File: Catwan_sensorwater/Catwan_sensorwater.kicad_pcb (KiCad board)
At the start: 2 copper layers, 40 parts, among them J1 SENSOR 1, J10 VSP, J2 SENSOR 2, J3 SENSOR 3, J4 BATT, J5 USB_B, J6 Conn_01x04, J7 Serial, J8 Conn_01x03_Female, J9 SENSOR 4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

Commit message: Inicio PCB
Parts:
- added U5: 74HC4052, Package_SO:SOIC-16_3.9x9.9mm_P1.27mm, F.Cu at (495.9, -68.6)
- J7: value Serial -> Conn_01x03; footprint TerminalBlock_Phoenix:TerminalBlock_Phoenix_PT-1,5-2-3.5-H_1x02_P3.50mm_Horizontal -> Connector_PinHeader_2.54mm:PinHeader_1x03_P2.54mm_Vertical
- U4: footprint Package_TO_SOT_SMD:SOT-223 -> Package_TO_SOT_SMD:SOT-23-5
- moved Q2 113.8 mm to (529.6, -58.4)
- moved Q4 98.4 mm to (518.2, -40.0)
- moved D10 86.8 mm to (495.9, -92.7)
- moved J3 81.3 mm to (511.2, -113.0)
- moved J8 80.7 mm to (520.7, -101.0)
- moved J1 79.4 mm to (505.5, -27.9)
- moved Q3 76.5 mm to (502.9, -65.4)
- moved R2 71.1 mm to (387.6, -97.2)
- moved J9 67.8 mm to (516.6, -75.6)
- moved D8 66.1 mm to (461.3, -101.0)
- moved J2 63.2 mm to (513.1, -61.0)
- moved C1 60.7 mm to (398.4, -55.9)
- moved C7 57.6 mm to (397.8, -88.9)
- moved SW1 57.3 mm to (398.8, -102.9)
- moved Q1 52.5 mm to (502.9, -51.4)
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
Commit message: acomodo
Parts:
- moved AE1 162.8 mm to (409.4, 30.4)
- moved C4 147.9 mm to (382.8, 44.5)
- moved J8 147.4 mm to (398.7, -18.3), turned to 90 degrees
- moved R2 144.3 mm to (462.7, 26.0), turned to 180 degrees
- moved C3 137.9 mm to (440.3, 45.5), turned to 90 degrees
- moved J3 128.4 mm to (481.1, 11.8), turned to 270 degrees
- moved C2 119.0 mm to (387.2, 13.0)
- moved C10 116.8 mm to (373.3, 34.0)
- moved C7 112.8 mm to (454.0, 8.90), turned to 90 degrees
- moved U4 112.2 mm to (456.8, 47.4)
- moved C9 104.6 mm to (373.0, 19.2)
- moved J5 104.2 mm to (409.8, -4.83), turned to 180 degrees
- moved R6 103.9 mm to (507.9, 19.9)
- moved U2 103.1 mm to (445.8, 6.60)
- moved Q2 100.6 mm to (470.8, 23.2), turned to 90 degrees
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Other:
- board outline added: 80 x 45 mm

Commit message: Acomodo segunda parte
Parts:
- moved C1 71.3 mm to (424.3, 30.2), turned to 90 degrees
- moved C6 70.4 mm to (449.8, 1.78)
- moved C4 68.2 mm to (433.2, -1.53), turned to 90 degrees
- moved R6 66.8 mm to (442.6, 6.22), turned to 90 degrees
- moved D10 61.1 mm to (435.1, 7.11)
- moved R4 56.3 mm to (460.3, -5.84)
- moved R3 54.0 mm to (454.1, -6.22)
- moved SW1 48.9 mm to (432.6, 30.9)
- moved D8 45.0 mm to (427.2, 6.48)
- moved U4 44.8 mm to (454.7, 2.60)
- moved C2 44.1 mm to (426.2, -7.75), turned to 90 degrees
- moved J8 43.7 mm to (440.9, -7.11)
- moved D9 36.9 mm to (418.6, 1.91)
- moved C5 25.2 mm to (433.2, -8.00), turned to 90 degrees
- moved J6 14.5 mm to (434.2, 23.9)
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
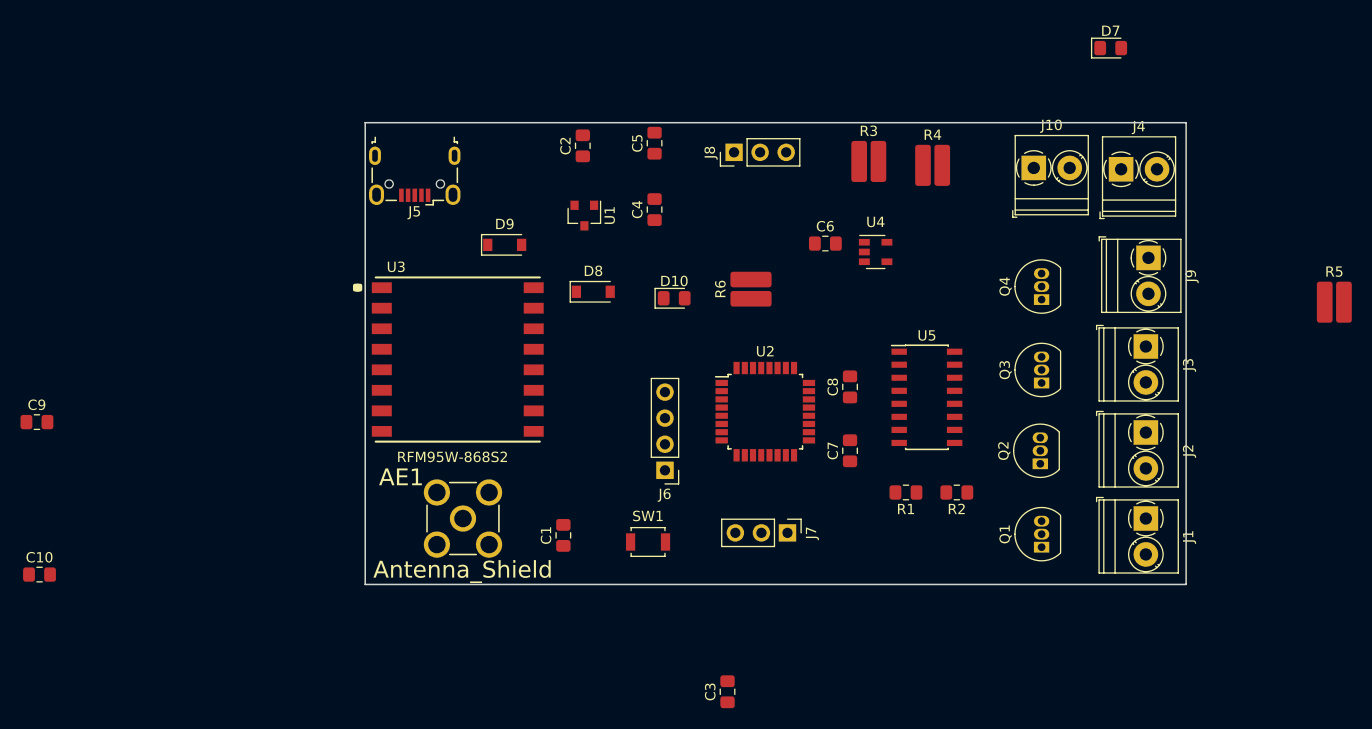
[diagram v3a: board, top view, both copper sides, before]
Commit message: Acomodo componentes
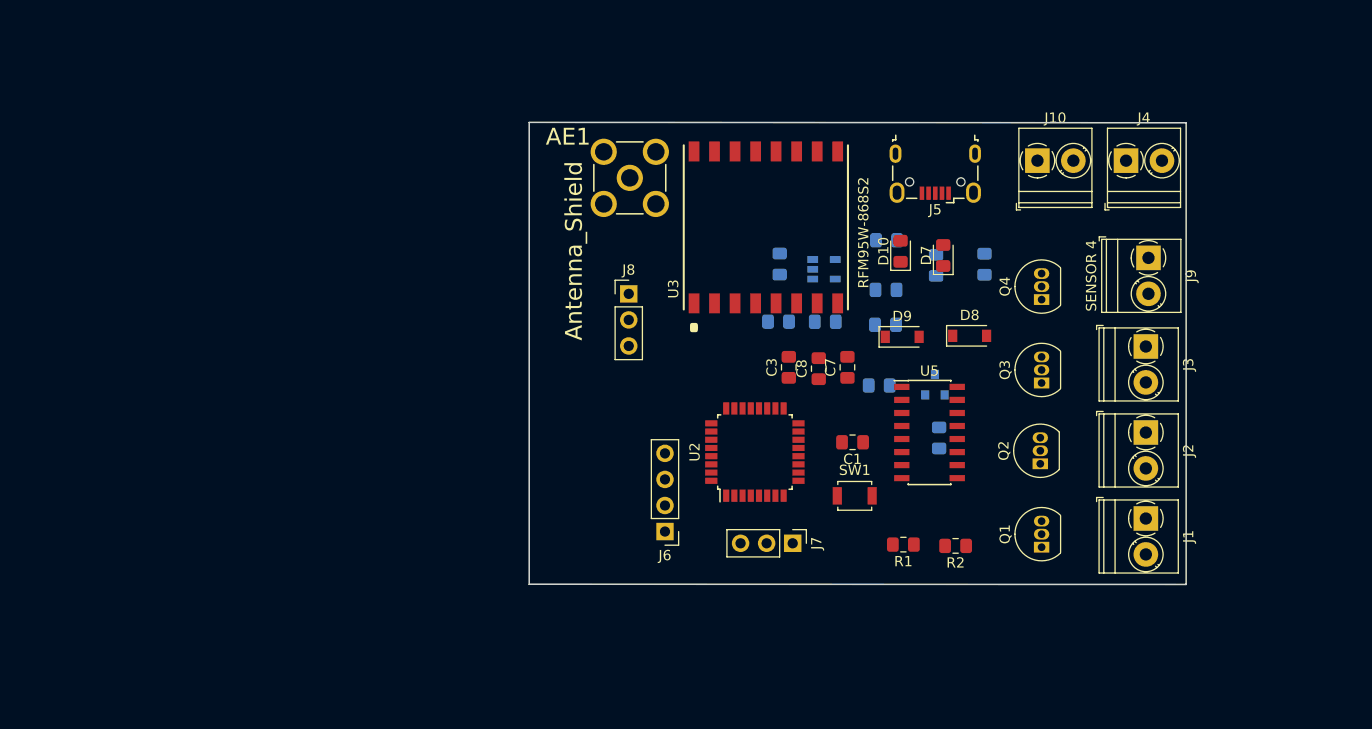
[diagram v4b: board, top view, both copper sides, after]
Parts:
- C10, C2, C4, C5, C6, C9, U1, U4: moved to B.Cu
- R3, R4, R5, R6: footprint Resistor_SMD:R_0815_2038Metric_Pad1.53x4.00mm_HandSolder -> Resistor_SMD:R_0805_2012Metric_Pad1.15x1.40mm_HandSolder; moved to B.Cu
- moved C10 96.9 mm to (465.4, 3.79), turned to 270 degrees
- moved C9 88.9 mm to (460.6, 3.90), turned to 270 degrees
- moved R5 54.2 mm to (445.3, 9.39)
- moved J5 50.7 mm to (460.6, -5.03)
- moved D9 39.8 mm to (457.3, 10.9)
- moved U1 37.9 mm to (460.5, 15.5), turned to 90 degrees
- moved AE1 37.0 mm to (430.8, -4.62)
- moved D8 36.9 mm to (463.9, 10.8)
- moved C4 35.6 mm to (460.9, 20.7)
- moved C2 34.3 mm to (455.7, 9.69), turned to 180 degrees
- moved U3 32.7 mm to (444.0, 0.20), turned to 90 degrees
- moved C3 32.2 mm to (446.3, 13.8)
- moved C1 29.6 mm to (452.5, 21.1), turned to 180 degrees
- moved C5 26.7 mm to (455.8, 6.29), turned to 180 degrees
- moved D7 26.0 mm to (461.3, 2.94), turned to 90 degrees
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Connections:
- U2 pad 29: +3V3 -> GND
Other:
- board size 80 x 45 mm -> 64 x 45 mm

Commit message: Rooteo
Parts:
- moved U3 2.60 mm to (445.7, 2.20), turned to 180 degrees
- moved AE1 0.64 mm to (431.4, -4.83), turned to 90 degrees
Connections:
- AE1 pad 4: (no net) -> GND
- AE1 pad 5: (no net) -> GND
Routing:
- net GND: track 0.00 -> 46.8 mm
- net /DHT_DAT: track 0.00 -> 28.3 mm
- net /DIO0: track 0.00 -> 26.5 mm
- net +3V3: track 0.00 -> 25.1 mm
- net /DIO1: track 0.00 -> 13.6 mm
- net /DIO2: track 0.00 -> 10.3 mm
- net Net-(AE1-Pad1): track 0.00 -> 6.93 mm
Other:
- net class Default: trace_width 0.25 -> 0.3; via_dia 0.8 -> 1
- net class SOURCE added: clearance 0.2, trace_width 0.5, via_dia 1.2, via_drill 0.6

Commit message: Segunda parte
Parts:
- U5: moved to B.Cu
- moved SW1 26.9 mm to (432.6, 8.49), turned to 180 degrees
- moved J7 20.2 mm to (426.5, 32.1), turned to 180 degrees
- moved R2 14.9 mm to (447.7, 30.7), turned to 270 degrees
- moved J6 11.6 mm to (426.4, 21.2)
- moved U5 7.64 mm to (459.1, 27.8)
- moved R1 6.31 mm to (451.1, 30.8), turned to 270 degrees
- moved J8 5.57 mm to (426.3, 3.19)
- moved U2 4.38 mm to (438.6, 22.1)
- moved Q1 4.31 mm to (471.2, 27.1), turned to 270 degrees
- moved Q3 3.60 mm to (470.8, 11.8), turned to 270 degrees
- moved Q4 3.56 mm to (470.8, 3.68), turned to 270 degrees
- moved Q2 2.87 mm to (471.2, 20.4), turned to 270 degrees
- moved U3 1.32 mm to (444.6, 1.55), turned to 90 degrees
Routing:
- net Net-(J3-Pad1): track 0.00 -> 37.2 mm
- net +3V3: track 25.1 -> 58.9 mm
- net Net-(J3-Pad2): track 0.00 -> 30.2 mm
- net /DHT_DAT: track 28.3 -> 0.00 mm
- net Net-(J2-Pad1): track 0.00 -> 27.2 mm
- net Net-(J2-Pad2): track 0.00 -> 20.8 mm
- net Net-(J1-Pad2): track 0.00 -> 20.3 mm
- net Net-(J1-Pad1): track 0.00 -> 19.8 mm
- net Net-(AE1-Pad1): track 6.93 -> 25.2 mm
- net /DIO2: track 10.3 -> 26.5 mm
- net /DIO5: track 0.00 -> 14.6 mm
- net /SCK: track 0.00 -> 14.6 mm
- net /DIO0: track 26.5 -> 12.3 mm
- net /RFM_RST: track 0.00 -> 12.1 mm
- net /DIO1: track 13.6 -> 25.5 mm
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
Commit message: distribution devices
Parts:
- D8, D9, R1, R2: moved to B.Cu
- R5, R6: moved to F.Cu
- moved J5 338.6 mm to (134.3, 85.8)
- moved C4 337.7 mm to (131.1, 93.3)
- moved C2 336.3 mm to (131.4, 98.6), turned to 90 degrees
- moved U1 334.2 mm to (135.5, 93.4), turned to 270 degrees
- moved C5 333.2 mm to (135.7, 98.7), turned to 90 degrees
- moved U3 331.5 mm to (130.3, 107.3), turned to 180 degrees
- moved D8 329.8 mm to (144.6, 93.2)
- moved J4 329.5 mm to (162.5, 84.9)
- moved J10 329.3 mm to (154.1, 84.8)
- moved J9 326.3 mm to (176.6, 120.0)
- moved Q4 325.3 mm to (167.2, 120.4)
- moved D10 325.0 mm to (145.0, 92.9), turned to 0 degrees
- moved C10 323.9 mm to (154.9, 96.3), turned to 0 degrees
- moved AE1 322.7 mm to (123.7, 92.6)
- moved D9 322.2 mm to (144.6, 88.5)
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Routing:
- net +3V3: track 58.9 -> 0.00 mm
- net /D+: track 0.00 -> 47.1 mm
- net /D-: track 0.00 -> 45.9 mm
- net GND: track 39.2 -> 0.00 mm
- net Net-(J3-Pad1): track 37.2 -> 0.00 mm
- net Net-(J3-Pad2): track 30.2 -> 0.00 mm
- net Net-(J2-Pad1): track 27.2 -> 0.00 mm
- net Net-(AE1-Pad1): track 25.2 -> 0.00 mm
- net Net-(J2-Pad2): track 20.8 -> 0.00 mm
- net Net-(J1-Pad2): track 20.3 -> 0.00 mm
- net Net-(J1-Pad1): track 19.8 -> 0.00 mm
- net /DIO0: track 12.3 -> 0.00 mm
- net Net-(J9-Pad1): track 11.2 -> 0.00 mm
- net Net-(J9-Pad2): track 10.7 -> 0.00 mm
- net /SCK: track 14.6 -> 7.47 mm
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
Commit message: change pcb
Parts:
- removed D8, D9: D_Zener, Diode_SMD:D_SOD-123
- added D1: D_Schottky, Diode_SMD:D_0805_2012Metric_Pad1.15x1.40mm_HandSolder, B.Cu at (105.8, 87.0)
- R1, R2, U5: moved to F.Cu
- U1: footprint Package_TO_SOT_SMD:SOT-23 -> Package_TO_SOT_SMD:SOT-223; moved to F.Cu
- moved C1 73.4 mm to (86.5, 99.2), turned to 270 degrees
- moved R4 69.3 mm to (93.0, 79.5)
- moved R3 65.2 mm to (97.8, 83.5)
- moved C6 61.8 mm to (102.2, 77.2)
- moved J4 60.5 mm to (114.0, 121.0)
- moved U4 55.9 mm to (99.1, 89.0), turned to 180 degrees
- moved C10 54.9 mm to (100.0, 94.5)
- moved C9 54.6 mm to (100.2, 97.5)
- moved J10 48.1 mm to (122.5, 121.0)
- moved C4 45.1 mm to (90.5, 113.0), turned to 270 degrees
- moved C5 43.8 mm to (94.2, 113.0), turned to 270 degrees
- moved C2 43.8 mm to (88.0, 92.5), turned to 270 degrees
- moved J5 35.2 mm to (135.2, 121.0), turned to 0 degrees
- moved U1 24.5 mm to (119.5, 112.0), turned to 90 degrees
- moved D7 22.7 mm to (143.5, 113.0)
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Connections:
- AE1 pad 4: GND -> (no net)
- AE1 pad 5: GND -> (no net)
- AE1 pad E: GND -> (no net)
- C4 pad 1: +3V3 -> Net-(C4-Pad1)
- J10 pad 2: VCC -> /Vsp
- U1 pad 3: +3V3 -> VCC
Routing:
- net /D+: track 47.1 -> 0.00 mm
- net /D-: track 45.9 -> 0.00 mm
- net /DIO2: track 32.4 -> 0.00 mm
- net /DIO1: track 29.4 -> 0.00 mm, vias 2 -> 0
- net /MOSI: track 14.6 -> 0.00 mm, vias 2 -> 0
- net /MIS0: track 10.6 -> 0.00 mm
- net /DIO5: track 8.03 -> 0.00 mm
- net /SCK: track 7.47 -> 0.00 mm
- net /SS: track 7.31 -> 0.00 mm
- net /RFM_RST: track 6.81 -> 0.00 mm
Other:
- board size 64 x 45 mm -> 79.9 x 45 mm
- net class SOURCE: trace_width 0.5 -> 1
